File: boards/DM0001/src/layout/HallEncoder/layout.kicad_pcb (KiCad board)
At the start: 2 copper layers, 14 parts, among them U1 BM05B-SRSS-TB

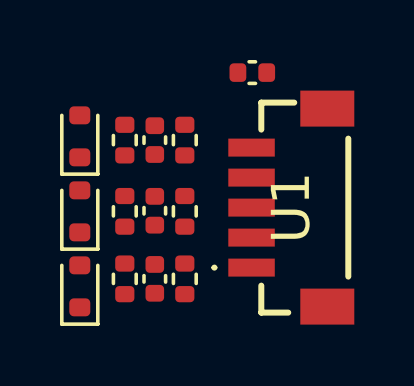
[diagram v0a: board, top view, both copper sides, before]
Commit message: remove ignored files
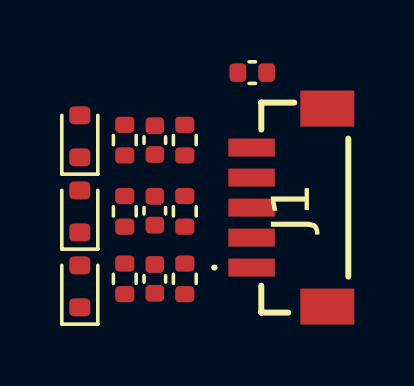
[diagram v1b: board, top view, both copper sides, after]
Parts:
- C4: value 100nF 16V -> 100nF 16V X7R
- renumbered U1 to J1
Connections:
- J1 pad MP1: GND -> MP1
- J1 pad MP2: GND -> MP2

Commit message: Sync layouts (#61)
* Sync reference design layouts

* Remove stale properties

* Update board layouts
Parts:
- C1, C2, C3: value 10pF 10V -> GCM1555C1H100FA16D
- C4: value 100nF 16V X7R -> GCM155R71H104KE02D
- J1: value BM05B-SRSS-TB -> BM05B-SRSS-TB(LF)(SN)
- R1, R2, R3, R4, R5, R6: value 10k -> ERJ-2RKF1002X
